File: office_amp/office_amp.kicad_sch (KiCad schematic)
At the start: 3 parts

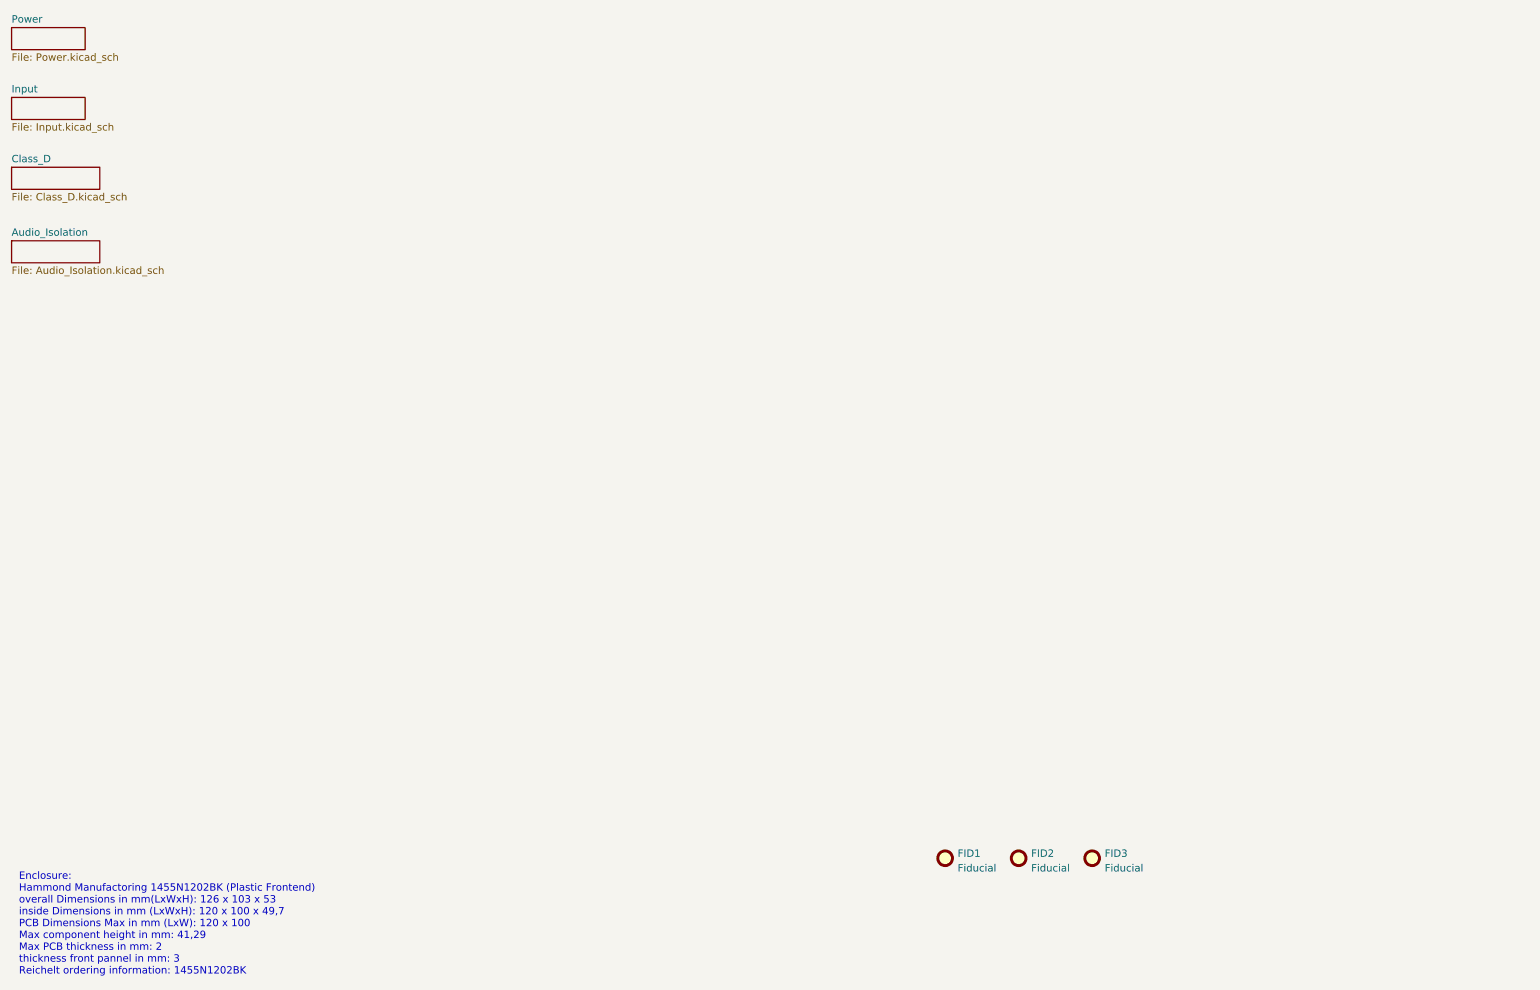
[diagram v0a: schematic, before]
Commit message: Organized Schematic
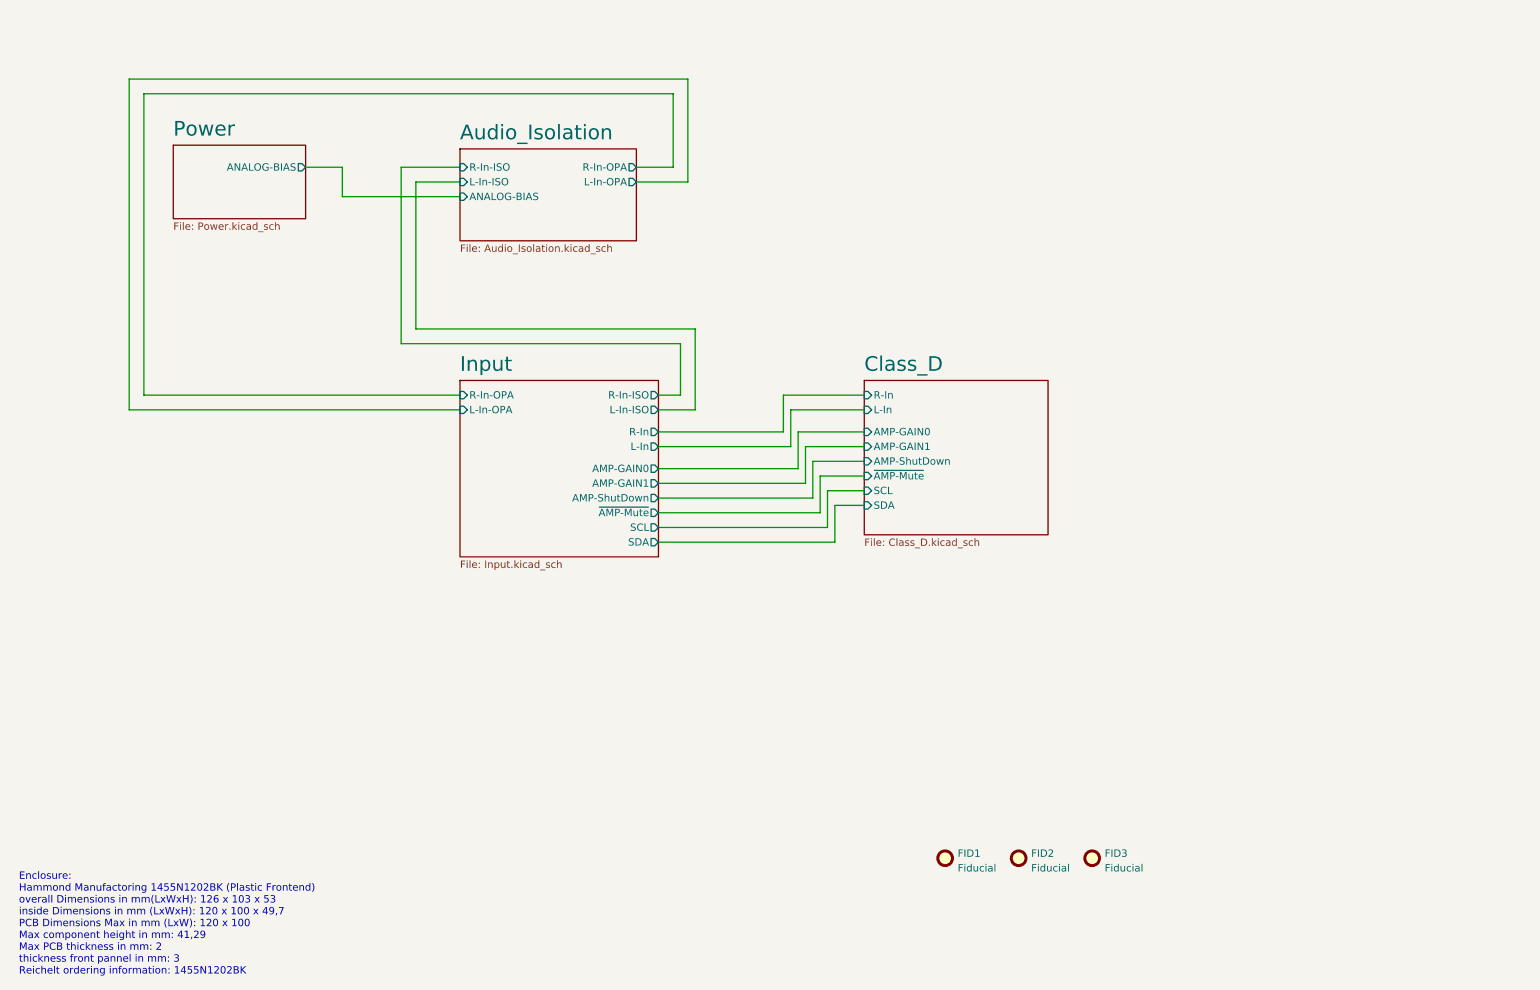
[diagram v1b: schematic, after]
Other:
- sheet Audio_Isolation ports: added ANALOG-BIAS, L-In-ISO, L-In-OPA, R-In-ISO, R-In-OPA; removed none
- sheet Class_D ports: added AMP-GAIN0, AMP-GAIN1, AMP-ShutDown, L-In, R-In, SCL, SDA, ~{AMP-Mute}; removed none
- sheet Input ports: added AMP-GAIN0, AMP-GAIN1, AMP-ShutDown, L-In, L-In-ISO, L-In-OPA, R-In, R-In-ISO, R-In-OPA, SCL, SDA, ~{AMP-Mute}; removed none
- sheet Power ports: added ANALOG-BIAS; removed none

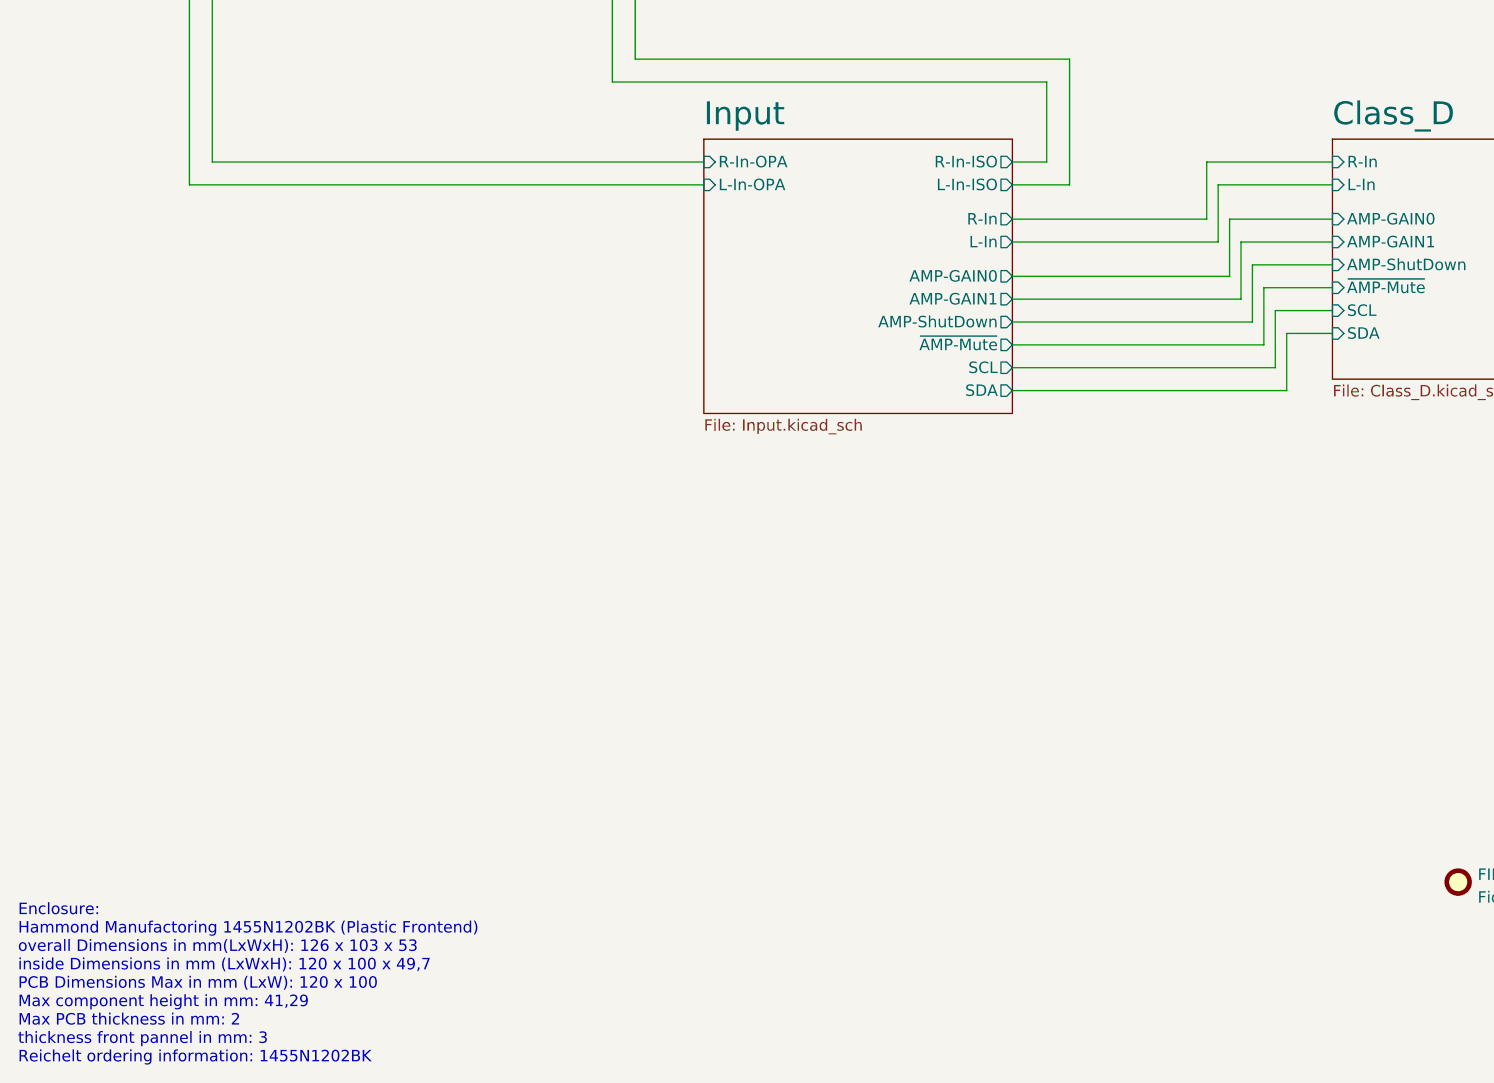
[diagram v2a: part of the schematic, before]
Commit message: error correction aftertest; corrected pinout touch; added level shifter for i2c poti; corrected voltages i2c poti
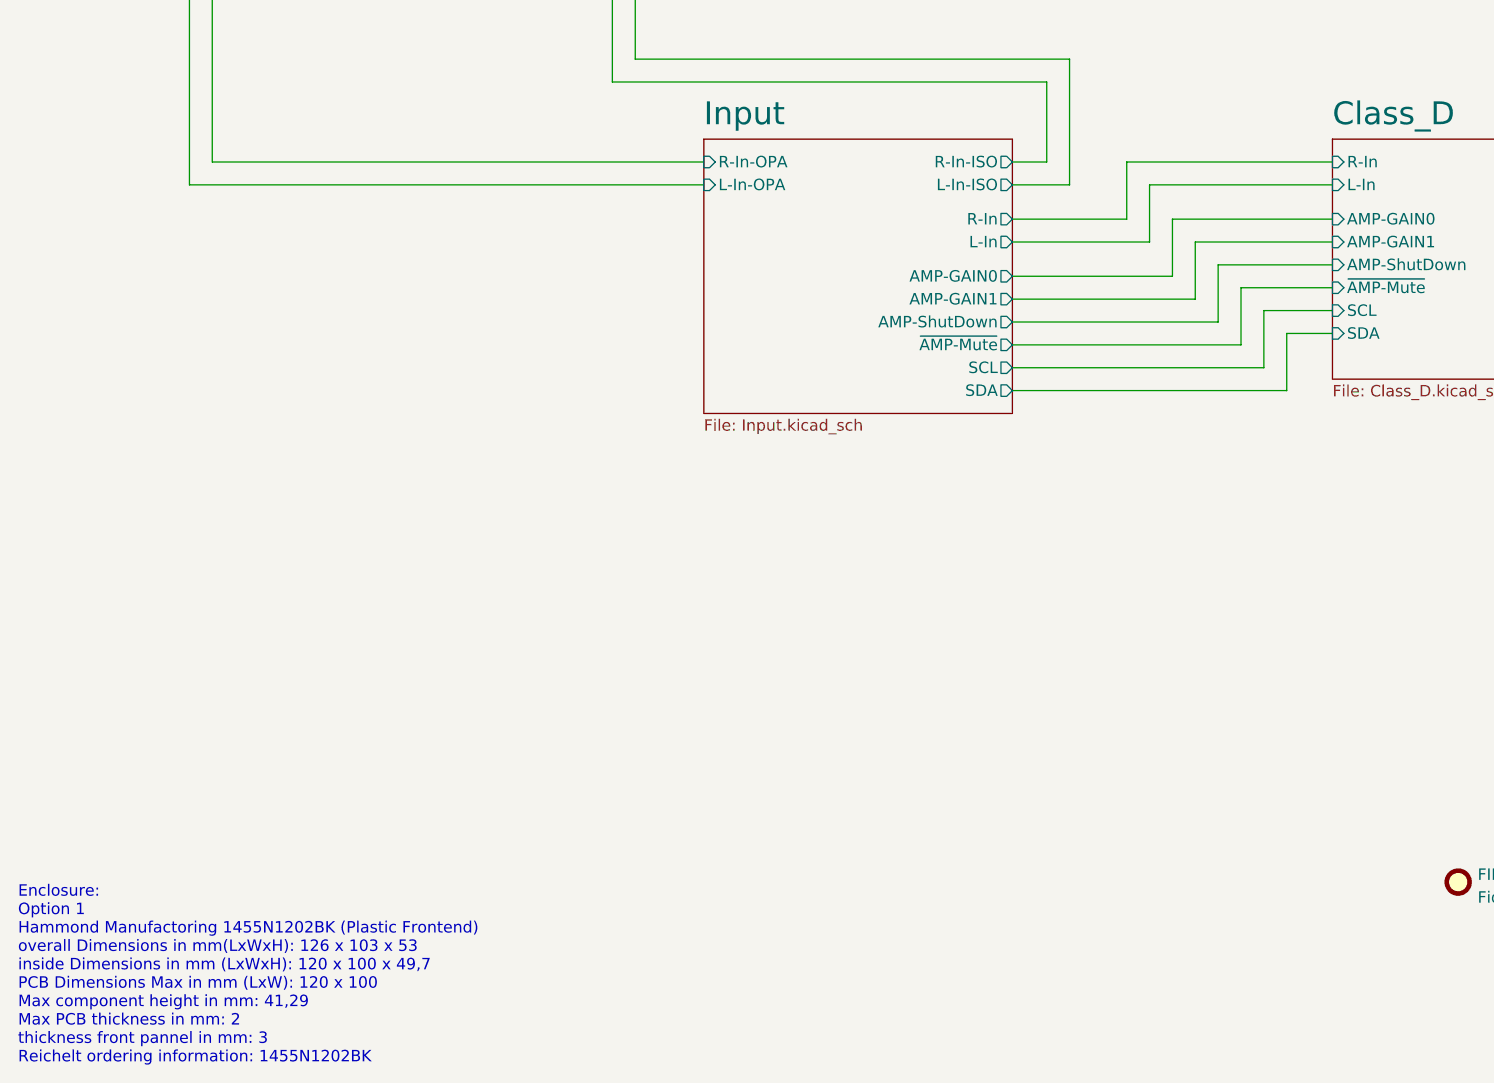
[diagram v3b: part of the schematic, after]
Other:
- note added: "Enclosure: Option 1 Hammond Manufactoring 1455N1202BK (Plastic Frontend) overall Dimensions in mm(LxWxH): 126 x 103 x 53 inside Dimensions in mm (LxWxH): 120 x 100 x 49,7 PCB Dimensions Max in mm (LxW): 120 x 100 Max component height in mm: 41,29 Max PCB thickness in mm: 2 thickness front pannel in mm: 3 Reichelt ordering information: 1455N1202BK"
- note removed: "Enclosure: Hammond Manufactoring 1455N1202BK (Plastic Frontend) overall Dimensions in mm(LxWxH): 126 x 103 x 53 inside Dimensions in mm (LxWxH): 120 x 100 x 49,7 PCB Dimensions Max in mm (LxW): 120 x 100 Max component height in mm: 41,29 Max PCB thickness in mm: 2 thickness front pannel in mm: 3 Reichelt ordering information: 1455N1202BK"
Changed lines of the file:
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@@
     (rev "1")
   )
-  (wire (pts (xy 156.21 101.6) (xy 156.21 95.25))
-    (stroke (width 0) (type default) (color 0 0 0 0))
-  )
-  (wire (pts (xy 157.48 97.79) (xy 163.83 97.79))
+  (wire (pts (xy 153.67 101.6) (xy 153.67 95.25))
+    (stroke (width 0) (type default) (color 0 0 0 0))
+  )
+  (wire (pts (xy 156.21 97.79) (xy 163.83 97.79))
     (stroke (width 0) (type default) (color 0 0 0 0))
   )
@@
     (stroke (width 0) (type default) (color 0 0 0 0))
   )
-  (wire (pts (xy 152.4 87.63) (xy 163.83 87.63))
+  (wire (pts (xy 146.05 87.63) (xy 163.83 87.63))
     (stroke (width 0) (type default) (color 0 0 0 0))
   )
@@
     (stroke (width 0) (type default) (color 0 0 0 0))
   )
-  (wire (pts (xy 153.67 96.52) (xy 153.67 90.17))
+  (wire (pts (xy 148.59 96.52) (xy 148.59 90.17))
     (stroke (width 0) (type default) (color 0 0 0 0))
   )
@@
     (stroke (width 0) (type default) (color 0 0 0 0))
   )
-  (wire (pts (xy 128.27 90.17) (xy 151.13 90.17))
+  (wire (pts (xy 128.27 90.17) (xy 143.51 90.17))
     (stroke (width 0) (type default) (color 0 0 0 0))
   )
@@
     (stroke (width 0) (type default) (color 0 0 0 0))
   )
-  (wire (pts (xy 128.27 87.63) (xy 149.86 87.63))
-    (stroke (width 0) (type default) (color 0 0 0 0))
-  )
-  (wire (pts (xy 153.67 90.17) (xy 163.83 90.17))
+  (wire (pts (xy 128.27 87.63) (xy 140.97 87.63))
+    (stroke (width 0) (type default) (color 0 0 0 0))
+  )
+  (wire (pts (xy 148.59 90.17) (xy 163.83 90.17))
     (stroke (width 0) (type default) (color 0 0 0 0))
   )
@@
     (stroke (width 0) (type default) (color 0 0 0 0))
   )
-  (wire (pts (xy 156.21 95.25) (xy 163.83 95.25))
+  (wire (pts (xy 153.67 95.25) (xy 163.83 95.25))
     (stroke (width 0) (type default) (color 0 0 0 0))
   )
@@
     (stroke (width 0) (type default) (color 0 0 0 0))
   )
-  (wire (pts (xy 128.27 99.06) (xy 154.94 99.06))
+  (wire (pts (xy 128.27 99.06) (xy 151.13 99.06))
     (stroke (width 0) (type default) (color 0 0 0 0))
   )
@@
     (stroke (width 0) (type default) (color 0 0 0 0))
   )
-  (wire (pts (xy 128.27 101.6) (xy 156.21 101.6))
+  (wire (pts (xy 128.27 101.6) (xy 153.67 101.6))
     (stroke (width 0) (type default) (color 0 0 0 0))
   )
@@
     (stroke (width 0) (type default) (color 0 0 0 0))
   )
-  (wire (pts (xy 149.86 81.28) (xy 163.83 81.28))
-    (stroke (width 0) (type default) (color 0 0 0 0))
-  )
-  (wire (pts (xy 152.4 93.98) (xy 152.4 87.63))
-    (stroke (width 0) (type default) (color 0 0 0 0))
-  )
-  (wire (pts (xy 157.48 104.14) (xy 157.48 97.79))
-    (stroke (width 0) (type default) (color 0 0 0 0))
-  )
-  (wire (pts (xy 151.13 90.17) (xy 151.13 83.82))
+  (wire (pts (xy 140.97 81.28) (xy 163.83 81.28))
+    (stroke (width 0) (type default) (color 0 0 0 0))
+  )
+  (wire (pts (xy 146.05 93.98) (xy 146.05 87.63))
+    (stroke (width 0) (type default) (color 0 0 0 0))
+  )
+  (wire (pts (xy 156.21 104.14) (xy 156.21 97.79))
+    (stroke (width 0) (type default) (color 0 0 0 0))
+  )
+  (wire (pts (xy 143.51 90.17) (xy 143.51 83.82))
     (stroke (width 0) (type default) (color 0 0 0 0))
   )
@@
     (stroke (width 0) (type default) (color 0 0 0 0))
   )
-  (wire (pts (xy 154.94 92.71) (xy 163.83 92.71))
+  (wire (pts (xy 151.13 92.71) (xy 163.83 92.71))
     (stroke (width 0) (type default) (color 0 0 0 0))
   )
@@
     (stroke (width 0) (type default) (color 0 0 0 0))
   )
-  (wire (pts (xy 151.13 83.82) (xy 163.83 83.82))
+  (wire (pts (xy 143.51 83.82) (xy 163.83 83.82))
     (stroke (width 0) (type default) (color 0 0 0 0))
   )
@@
     (stroke (width 0) (type default) (color 0 0 0 0))
   )
-  (wire (pts (xy 149.86 87.63) (xy 149.86 81.28))
-    (stroke (width 0) (type default) (color 0 0 0 0))
-  )
-  (wire (pts (xy 128.27 96.52) (xy 153.67 96.52))
+  (wire (pts (xy 140.97 87.63) (xy 140.97 81.28))
+    (stroke (width 0) (type default) (color 0 0 0 0))
+  )
+  (wire (pts (xy 128.27 96.52) (xy 148.59 96.52))
     (stroke (width 0) (type default) (color 0 0 0 0))
   )
@@
     (stroke (width 0) (type default) (color 0 0 0 0))
   )
-  (wire (pts (xy 128.27 93.98) (xy 152.4 93.98))
-    (stroke (width 0) (type default) (color 0 0 0 0))
-  )
-  (wire (pts (xy 128.27 104.14) (xy 157.48 104.14))
-    (stroke (width 0) (type default) (color 0 0 0 0))
-  )
-  (wire (pts (xy 154.94 99.06) (xy 154.94 92.71))
+  (wire (pts (xy 128.27 93.98) (xy 146.05 93.98))
+    (stroke (width 0) (type default) (color 0 0 0 0))
+  )
+  (wire (pts (xy 128.27 104.14) (xy 156.21 104.14))
+    (stroke (width 0) (type default) (color 0 0 0 0))
+  )
+  (wire (pts (xy 151.13 99.06) (xy 151.13 92.71))
     (stroke (width 0) (type default) (color 0 0 0 0))
   )
@@
     (stroke (width 0) (type default) (color 0 0 0 0))
   )
-  (text "Enclosure:\nHammond Manufactoring 1455N1202BK (Plastic Frontend)\noverall Dimensions in mm(LxWxH): 126 x 103 x 53\ninside Dimensions in mm (LxWxH): 120 x 100 x 49,7\nPCB Dimensions Max in mm (LxW): 120 x 100\nMax component height in mm: 41,29\nMax PCB thickness in mm: 2\nthickness front pannel in mm: 3\nReichelt ordering information: 1455N1202BK"
+  (text "Enclosure:\nOption 1\nHammond Manufactoring 1455N1202BK (Plastic Frontend)\noverall Dimensions in mm(LxWxH): 126 x 103 x 53\ninside Dimensions in mm (LxWxH): 120 x 100 x 49,7\nPCB Dimensions Max in mm (LxW): 120 x 100\nMax component height in mm: 41,29\nMax PCB thickness in mm: 2\nthickness front pannel in mm: 3\nReichelt ordering information: 1455N1202BK"
     (at 17.78 181.61 0)
     (effects (font (size 1.27 1.27)) (justify left bottom))
@@
       (reference "#PWR020") (unit 1) (value "GNDREF") (footprint "")
     )
+    (path "/00000000-0000-0000-0000-00005ed110e5/d1a74c5b-21cd-400a-9a66-db68ab525519"
+      (reference "#PWR021") (unit 1) (value "GNDREF") (footprint "")
+    )
     (path "/00000000-0000-0000-0000-00005ec853eb/1d9b0446-65b6-4db6-a887-8216cfa0063a"
       (reference "#PWR022") (unit 1) (value "GNDD") (footprint "")
@@
       (reference "#PWR039") (unit 1) (value "GND_Input") (footprint "")
     )
+    (path "/00000000-0000-0000-0000-0000602bbdaa/ab443cf4-1891-4813-8787-d760b3235efa"
+      (reference "#PWR040") (unit 1) (value "+5V") (footprint "")
+    )
     (path "/00000000-0000-0000-0000-0000602bbdaa/7a68d117-844f-4646-9d92-96b00c9725c6"
       (reference "#PWR042") (unit 1) (value "GNDREF") (footprint "")
@@
       (reference "#PWR058") (unit 1) (value "+5V") (footprint "")
     )
-    (path "/00000000-0000-0000-0000-0000602bbdaa/fb100677-1699-4437-ad8e-2cf161f9071e"
-      (reference "#PWR063") (unit 1) (value "+3V3") (footprint "")
-    )
     (path "/00000000-0000-0000-0000-00005ec853eb/00000000-0000-0000-0000-00005ec94916"
       (reference "#PWR0101") (unit 1) (value "GNDREF") (footprint "")
@@
       (reference "#PWR0137") (unit 1) (value "5V_BT") (footprint "")
     )
-    (path "/00000000-0000-0000-0000-00005ed110e5/d1a74c5b-21cd-400a-9a66-db68ab525519"
-      (reference "#PWR?") (unit 1) (value "GNDREF") (footprint "")
-    )
     (path "/00000000-0000-0000-0000-00005ec853eb/00000000-0000-0000-0000-00005ec94909"
       (reference "C1") (unit 1) (value "22nF") (footprint "Capacitor_SMD:C_0805_2012Metric_Pad1.18x1.45mm_HandSolder")
@@
       (reference "Q9") (unit 1) (value "BC856") (footprint "Package_TO_SOT_SMD:SOT-23")
     )
+    (path "/00000000-0000-0000-0000-0000602bbdaa/b1360983-9928-447a-b872-1b3b0540c61a"
+      (reference "Q10") (unit 1) (value "BSS138") (footprint "Package_TO_SOT_SMD:SOT-23")
+    )
+    (path "/00000000-0000-0000-0000-0000602bbdaa/d8d4c38a-636e-4f94-a112-6b2e83edd051"
+      (reference "Q11") (unit 1) (value "BSS138") (footprint "Package_TO_SOT_SMD:SOT-23")
+    )
     (path "/00000000-0000-0000-0000-0000602bbdaa/00000000-0000-0000-0000-000060317764"
       (reference "R1") (unit 1) (value "10K") (footprint "Resistor_SMD:R_0805_2012Metric_Pad1.20x1.40mm_HandSolder")
@@
       (reference "R37") (unit 1) (value "?") (footprint "Resistor_SMD:R_0805_2012Metric_Pad1.20x1.40mm_HandSolder")
     )
+    (path "/00000000-0000-0000-0000-0000602bbdaa/12ed6d75-d19f-4671-afdc-66f2d07914c3"
+      (reference "R38") (unit 1) (value "10k") (footprint "Resistor_SMD:R_0805_2012Metric_Pad1.20x1.40mm_HandSolder")
+    )
+    (path "/00000000-0000-0000-0000-0000602bbdaa/1e981756-bc01-4514-a059-490b4bdf3b7a"
+      (reference "R39") (unit 1) (value "10k") (footprint "Resistor_SMD:R_0805_2012Metric_Pad1.20x1.40mm_HandSolder")
+    )
     (path "/00000000-0000-0000-0000-000060794134/00000000-0000-0000-0000-00006084cc9d"
